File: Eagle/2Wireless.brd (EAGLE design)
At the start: 62.7 x 31.8 mm, 18 parts, among them IC1 TCA9517A, IC2 VREGLD1117, IC3 MB85RS256TYPNF-G-BCERE1, U1 PHOTON_WITH_HEADERS

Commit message: Change FRAM to 256k.
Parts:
- IC3: value MB85RS256TYPNF-G-BCERE1 -> MB85RS2MTAPNF-G-BDERE1
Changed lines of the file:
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@@
 <attribute name="NAME" x="59.336" y="29.116" size="1.27" layer="21" rot="R270"/>
 </element>
-<element name="IC3" library="studio_h" package="SO08" value="MB85RS256TYPNF-G-BCERE1" x="46.482" y="19.304" smashed="yes">
+<element name="IC3" library="studio_h" package="SO08" value="MB85RS2MTAPNF-G-BDERE1" x="46.482" y="19.304" smashed="yes">
 <attribute name="Z_MOUSER" value="" x="46.482" y="19.304" size="1.778" layer="27" display="off"/>
 <attribute name="Z_SMT" value="Y" x="46.482" y="19.304" size="1.778" layer="27" display="off"/>
 <attribute name="MF" value="FUJITSU" x="46.482" y="19.304" size="1.778" layer="27" display="off"/>
-<attribute name="MPN" value="MB85RS256TYPNF-G-BCERE1" x="46.482" y="19.304" size="1.778" layer="27" display="off"/>
-<attribute name="Z_DIGIKEY" value="865-1293-1-ND" x="46.482" y="19.304" size="1.778" layer="27" display="off"/>
-<attribute name="VALUE" x="50.419" y="17.272" size="1.27" layer="27" font="vector" ratio="12" rot="R90"/>
+<attribute name="MPN" value="MB85RS2MTAPNF-G-BDERE1" x="46.482" y="19.304" size="1.778" layer="27" display="off"/>
+<attribute name="Z_DIGIKEY" value="865-1286-1-ND" x="46.482" y="19.304" size="1.778" layer="27" display="off"/>
+<attribute name="VALUE" value="MB85RS2MTAPNF-G-BDERE1" x="50.419" y="17.272" size="1.27" layer="27" font="vector" ratio="12" rot="R90"/>
 <attribute name="NAME" x="45.085" y="13.335" size="1.27" layer="25" font="vector" ratio="12"/>
 </element>

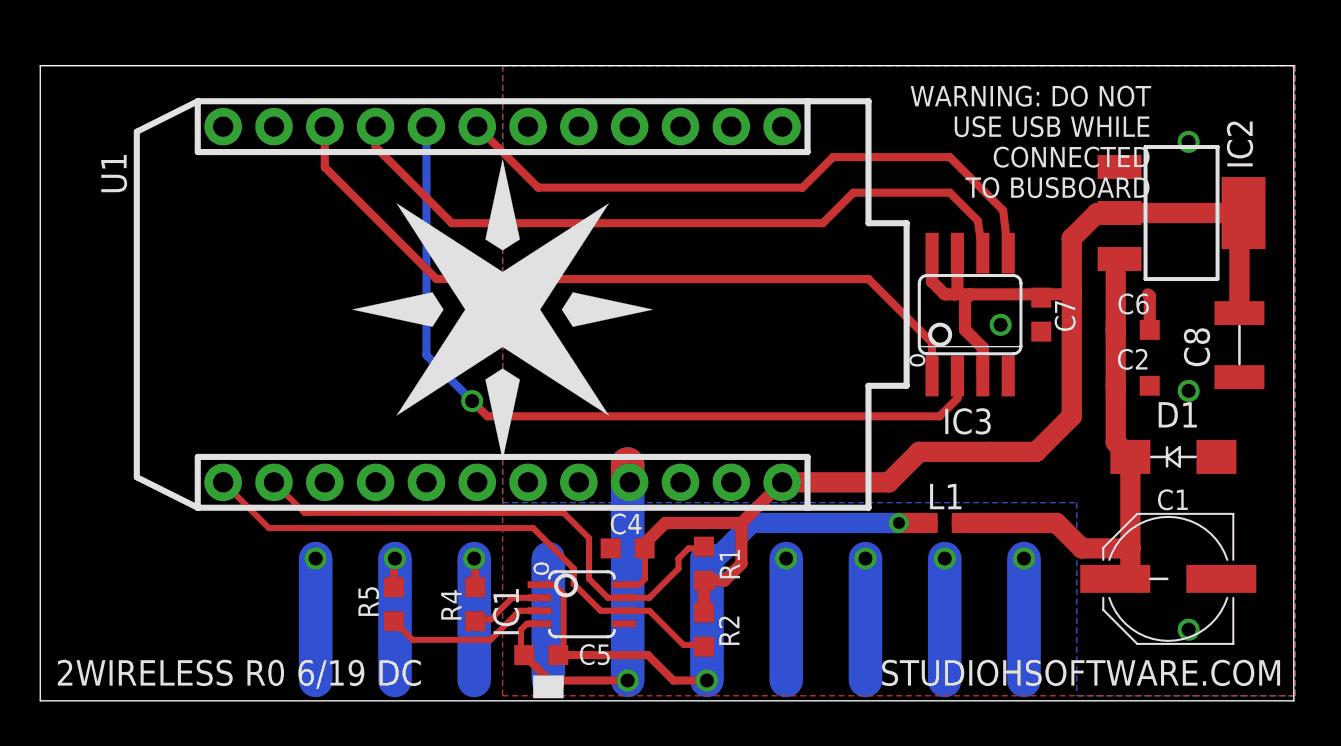
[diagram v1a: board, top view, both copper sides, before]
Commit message: Added two 24FC512. Photon unreliable as I2C slave.
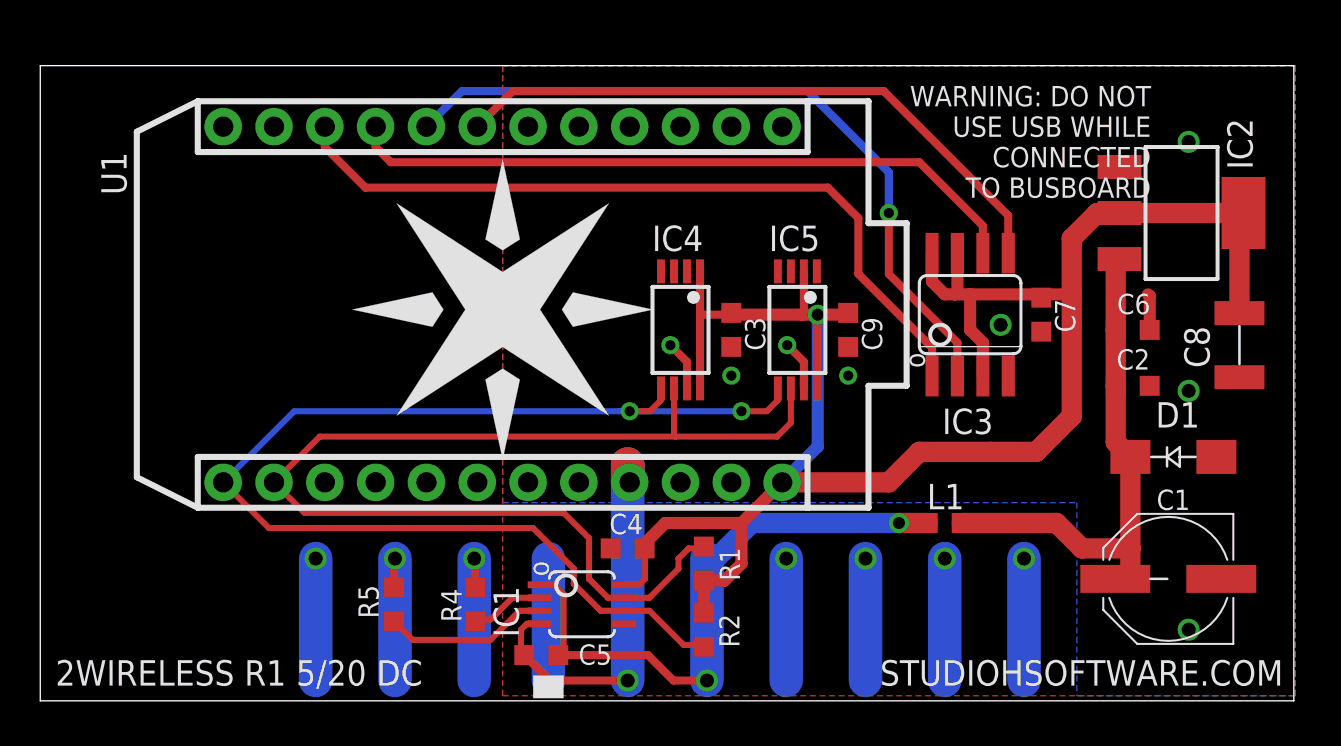
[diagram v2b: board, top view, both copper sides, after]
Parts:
- added C3, C9: 100n, studio_h:C0603
- added IC4, IC5: 24FC512, studio_h:TSSOP8
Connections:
- net DGND: now also C3.2, C9.2, IC4.2, IC4.3, IC4.4, IC4.7, IC5.1, IC5.3, IC5.4, IC5.7
- net DPWR: now also C3.1, C9.1, IC4.1, IC4.8, IC5.2, IC5.8
- net SCL: now also IC4.6, IC5.6
- net SDA: now also IC4.5, IC5.5
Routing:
- net SDA: track 27.9 -> 60.3 mm, vias 0 -> 2
- net SCL: track 26.4 -> 57.7 mm
- net DPWR: track 71.7 -> 99.9 mm, vias 0 -> 1
- net DGND: track 21.8 -> 27.9 mm, vias 5 -> 9
- net MISO: track 40.7 -> 37.1 mm
- net SCK: track 35.5 -> 34.4 mm
- net !CS: track 37.7 -> 38.6 mm
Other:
- board text added: "2WIRELESS R1 5/20 DC"
- board text removed: "2WIRELESS R0 6/19 DC"

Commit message: Add two more 24FC512.
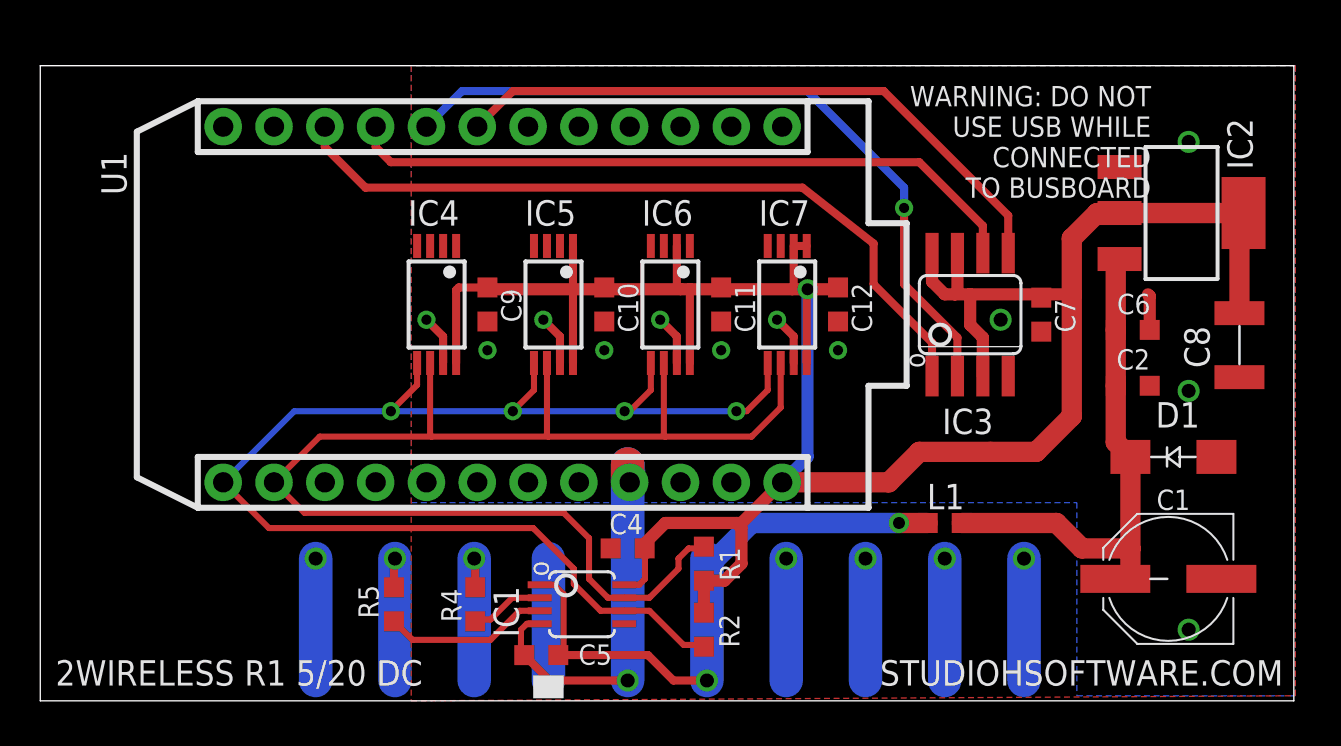
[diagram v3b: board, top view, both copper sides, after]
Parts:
- removed C3: 100n, studio_h:C0603
- removed U$1: (no value), Particle:PARTICLE_LOGO_15MM
- added C10, C11, C12: 100n, studio_h:C0603
- added IC6, IC7: 24FC512, studio_h:TSSOP8
- added U$2: (no value), Particle:SPARK_LOGO
- moved C9 18.1 mm to (22.4, 19.8)
- moved IC4 12.3 mm to (19.8, 19.8)
- moved IC5 12.3 mm to (25.7, 19.8)
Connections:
- net DGND: now also C10.2, C11.2, C12.2, IC4.1, IC5.2, IC6.1, IC6.3, IC6.4, IC6.7, IC7.3, IC7.4, IC7.7; no longer C3.2, IC5.1
- net DPWR: now also C10.1, C11.1, C12.1, IC5.1, IC6.2, IC6.8, IC7.1, IC7.2, IC7.8; no longer C3.1, IC4.1, IC5.2
- net SCL: now also IC6.6, IC7.6
- net SDA: now also IC6.5, IC7.5
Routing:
- net DPWR: track 99.9 -> 124.7 mm
- net SCL: track 57.7 -> 66.7 mm
- net SDA: track 60.3 -> 67.3 mm, vias 2 -> 4
- net DGND: track 27.9 -> 32.9 mm, vias 9 -> 13

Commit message: Remove 24FC512 chips. Not needed.
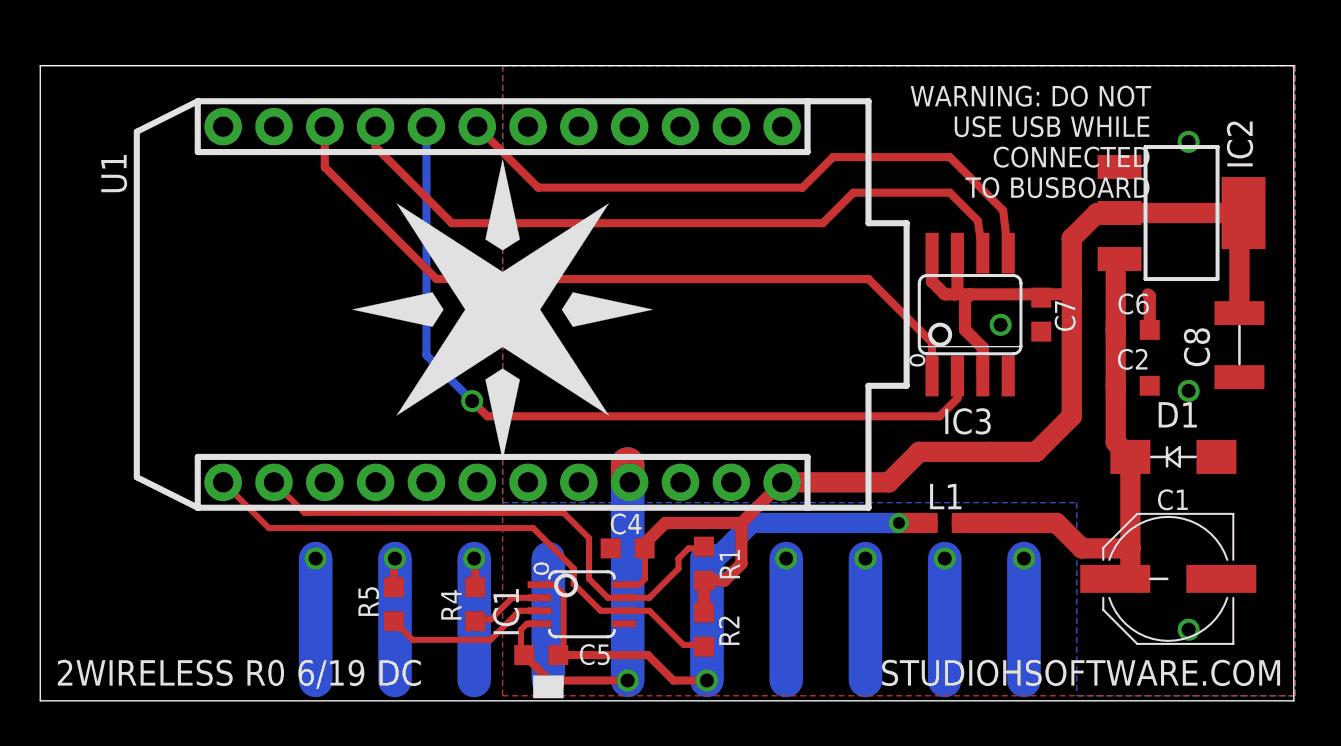
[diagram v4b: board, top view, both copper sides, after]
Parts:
- removed C10, C11, C12, C9: 100n, studio_h:C0603
- removed IC4, IC5, IC6, IC7: 24FC512, studio_h:TSSOP8
- removed U$2: (no value), Particle:SPARK_LOGO
- added U$1: (no value), Particle:PARTICLE_LOGO_15MM
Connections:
- net DGND: no longer C10.2, C11.2, C12.2, C9.2, IC4.1, IC4.2, IC4.3, IC4.4, IC4.7, IC5.2, IC5.3, IC5.4, IC5.7, IC6.1, IC6.3, IC6.4, IC6.7, IC7.3, IC7.4, IC7.7
- net DPWR: no longer C10.1, C11.1, C12.1, C9.1, IC4.8, IC5.1, IC5.8, IC6.2, IC6.8, IC7.1, IC7.2, IC7.8
- net SCL: no longer IC4.6, IC5.6, IC6.6, IC7.6
- net SDA: no longer IC4.5, IC5.5, IC6.5, IC7.5
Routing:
- net DPWR: track 124.7 -> 71.7 mm, vias 1 -> 0
- net SCL: track 66.7 -> 26.4 mm
- net SDA: track 67.3 -> 27.9 mm, vias 4 -> 0
- net DGND: track 32.9 -> 21.8 mm, vias 13 -> 5
- net MISO: track 37.1 -> 40.7 mm
- net SCK: track 34.4 -> 35.5 mm
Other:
- board text added: "2WIRELESS R0 6/19 DC"
- board text removed: "2WIRELESS R1 5/20 DC"

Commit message: Add Primo/V2 version switch.
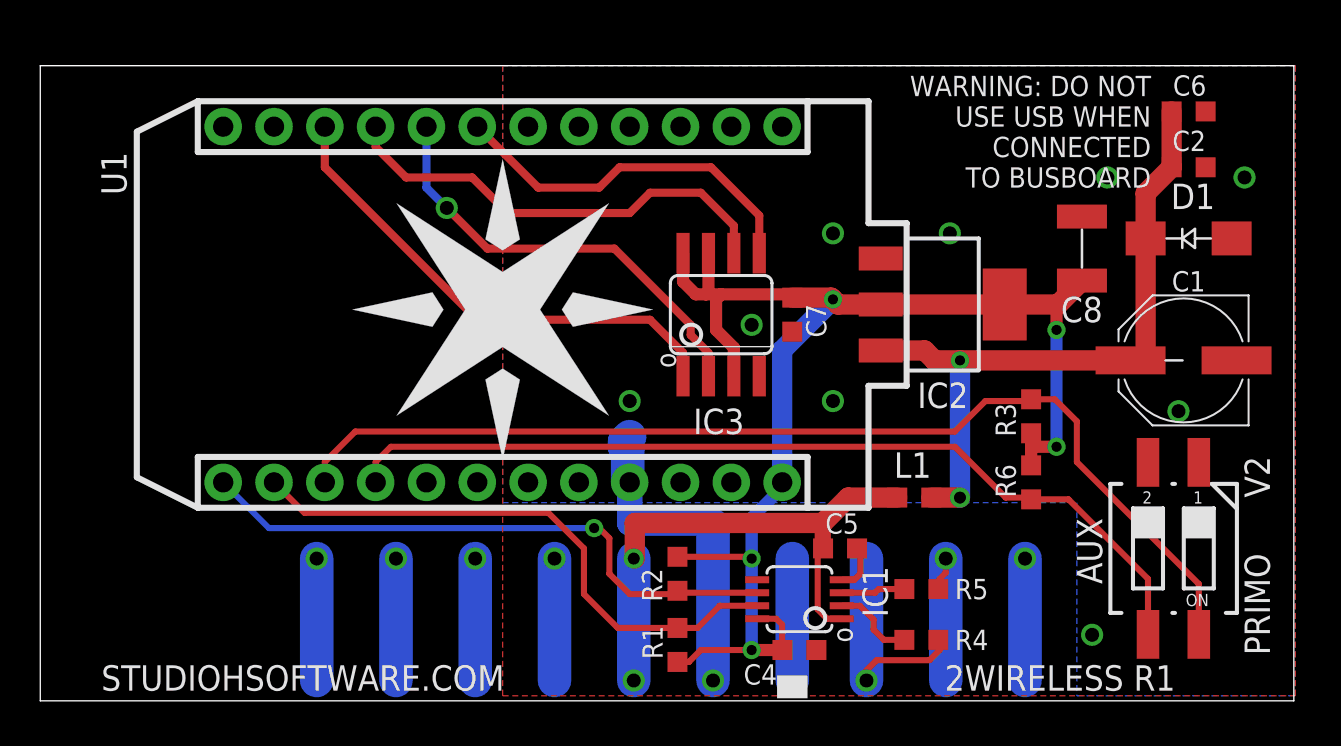
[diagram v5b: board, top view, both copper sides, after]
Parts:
- added R3, R6: 100k, studio_h:R0603
- added S1: DIP, studio_h:CTS-219-02
- moved R5 26.4 mm to (44.0, 5.59), turned to 0 degrees
- moved R4 22.4 mm to (44.0, 3.05), turned to 0 degrees
- moved C5 15.9 mm to (40.0, 7.62), turned to 0 degrees
- moved IC2 12.8 mm to (45.2, 19.8)
- moved C7 12.4 mm to (37.6, 19.3)
- moved IC3 12.4 mm to (34.0, 19.3)
- moved C2 11.3 mm to (57.4, 26.7)
- moved C6 11.3 mm to (57.4, 29.5)
- moved C1 10.9 mm to (57.1, 17.0)
- moved D1 10.9 mm to (57.4, 23.1)
- moved IC1 10.9 mm to (37.9, 5.08), turned to 90 degrees
- moved C4 9.98 mm to (37.9, 2.54), turned to 0 degrees
- moved C8 9.24 mm to (52.1, 22.6), turned to 90 degrees
- moved R1 4.27 mm to (31.9, 2.79)
- moved R2 3.09 mm to (31.9, 6.35)
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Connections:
- new net DI-AUX: R6.1, S1.3, U1.16
- new net DI-VERSION: R3.1, S1.4, U1.15
- net DGND: now also S1.1, S1.2
- net DPWR: now also R3.2, R6.2
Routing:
- net DI-VERSION: track 0.00 -> 53.5 mm
- net DI-AUX: track 0.00 -> 45.5 mm
- net MISO: track 40.7 -> 22.0 mm
- net SCK: track 35.5 -> 22.8 mm
- net MOSI: track 31.4 -> 18.7 mm
- net !CS: track 37.7 -> 24.9 mm
- net +5V: track 26.0 -> 34.6 mm, vias 0 -> 2
- net N$138: track 8.27 -> 3.21 mm
- net EDAC-I2C-CLK: track 7.55 -> 11.2 mm
- net EDAC-5V+: track 31.0 -> 27.9 mm
- net DGND: track 21.8 -> 18.8 mm, vias 5 -> 10
- net SCL: track 26.4 -> 29.0 mm
- net SDA: track 27.9 -> 30.2 mm, vias 0 -> 1
- net DPWR: track 71.7 -> 70.9 mm, vias 0 -> 5
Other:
- board text added: "2WIRELESS R1"
- board text added: "AUX"
- board text added: "PRIMO"
- board text added: "V2"
- board text added: "WARNING: DO NOT USE USB WHEN CONNECTED TO BUSBOARD"
- board text removed: "2WIRELESS R0 6/19 DC"
- board text removed: "WARNING: DO NOT USE USB WHILE CONNECTED TO BUSBOARD"

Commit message: Add RS232 Connector for future use.
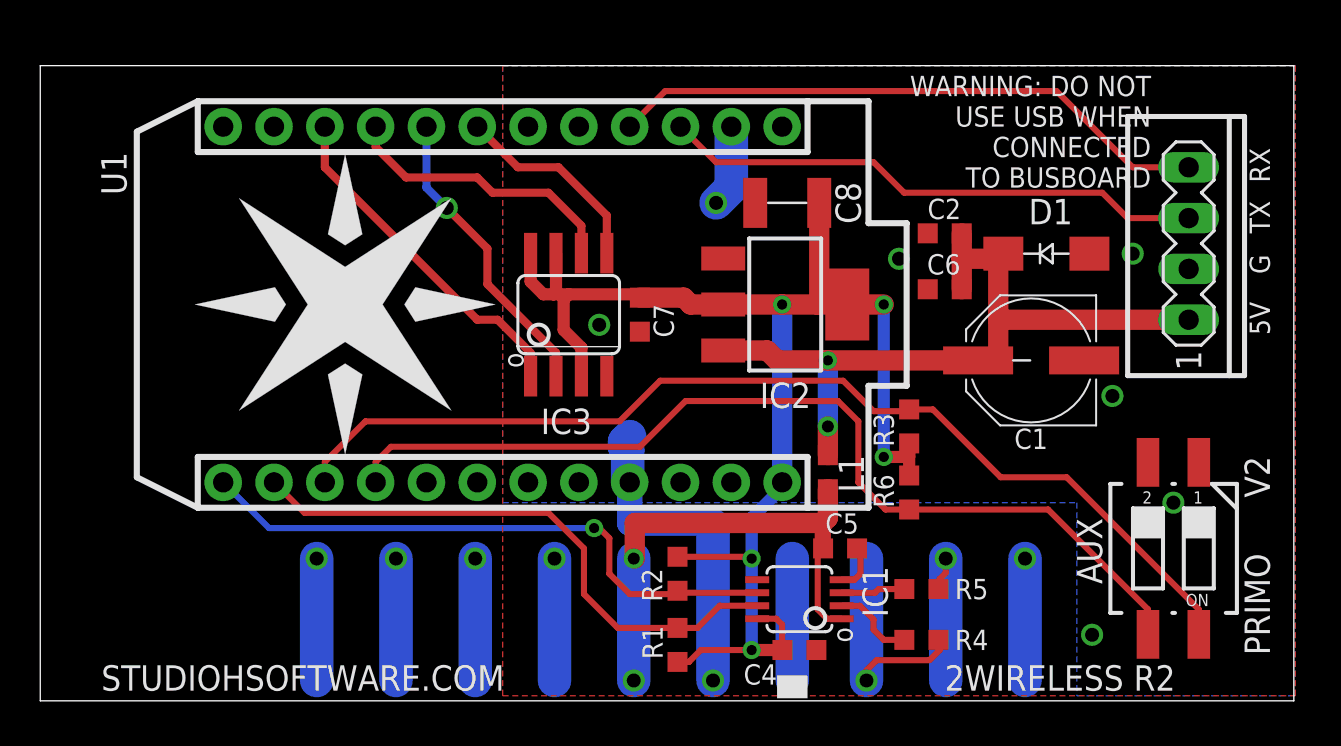
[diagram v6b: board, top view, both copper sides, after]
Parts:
- added SV1: (no value), studio_h:MA04-1
- moved C6 15.1 mm to (45.2, 20.6), turned to 180 degrees
- moved C8 14.9 mm to (37.3, 24.9), turned to 180 degrees
- moved C2 12.6 mm to (45.2, 23.4), turned to 180 degrees
- moved U$1 7.88 mm to (15.2, 19.8)
- moved IC2 7.87 mm to (37.3, 19.8)
- moved IC3 7.62 mm to (26.4, 19.3)
- moved C1 7.62 mm to (49.5, 17.0)
- moved C7 7.62 mm to (30.0, 19.3)
- moved D1 7.15 mm to (50.3, 22.4)
- moved R3 6.12 mm to (43.4, 13.7)
- moved R6 6.12 mm to (43.4, 10.4)
- moved L1 4.50 mm to (39.4, 11.4), turned to 90 degrees
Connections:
- new net RX: SV1.4, U1.4
- new net TX: SV1.3, U1.3
- net +5V: now also SV1.1
- net DGND: now also SV1.2
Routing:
- net RX: track 0.00 -> 30.3 mm
- net TX: track 0.00 -> 27.3 mm
- net MOSI: track 18.7 -> 10.2 mm
- net SCK: track 22.8 -> 14.3 mm
- net !CS: track 24.9 -> 17.3 mm
- net MISO: track 22.0 -> 15.2 mm
- net DGND: track 18.8 -> 23.0 mm, vias 10 -> 8
- net DI-AUX: track 45.5 -> 48.9 mm
- net +5V: track 34.6 -> 38.0 mm
- net EDAC-5V+: track 27.9 -> 25.4 mm
- net DPWR: track 70.9 -> 72.4 mm
- net DI-VERSION: track 53.5 -> 52.4 mm
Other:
- board text added: "2WIRELESS R2"
- board text added: "5V"
- board text added: "G"
- board text added: "RX"
- board text added: "TX"
- board text removed: "2WIRELESS R1"
